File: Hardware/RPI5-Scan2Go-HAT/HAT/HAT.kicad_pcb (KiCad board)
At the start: 2 copper layers, 76 x 96.5 mm, 35 parts, among them J1 RPi_GPIO, J10 Conn_01x02_Socket, J12 Conn_01x02_Socket, J13 Conn_01x02_Socket, J14 Conn_01x02_Socket, J15 Jack-DC 5V, J18 Conn_01x02_Socket, J19 Conn_01x02_Socket, J2 Conn_01x04_Socket, J20 Conn_01x05_Socket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

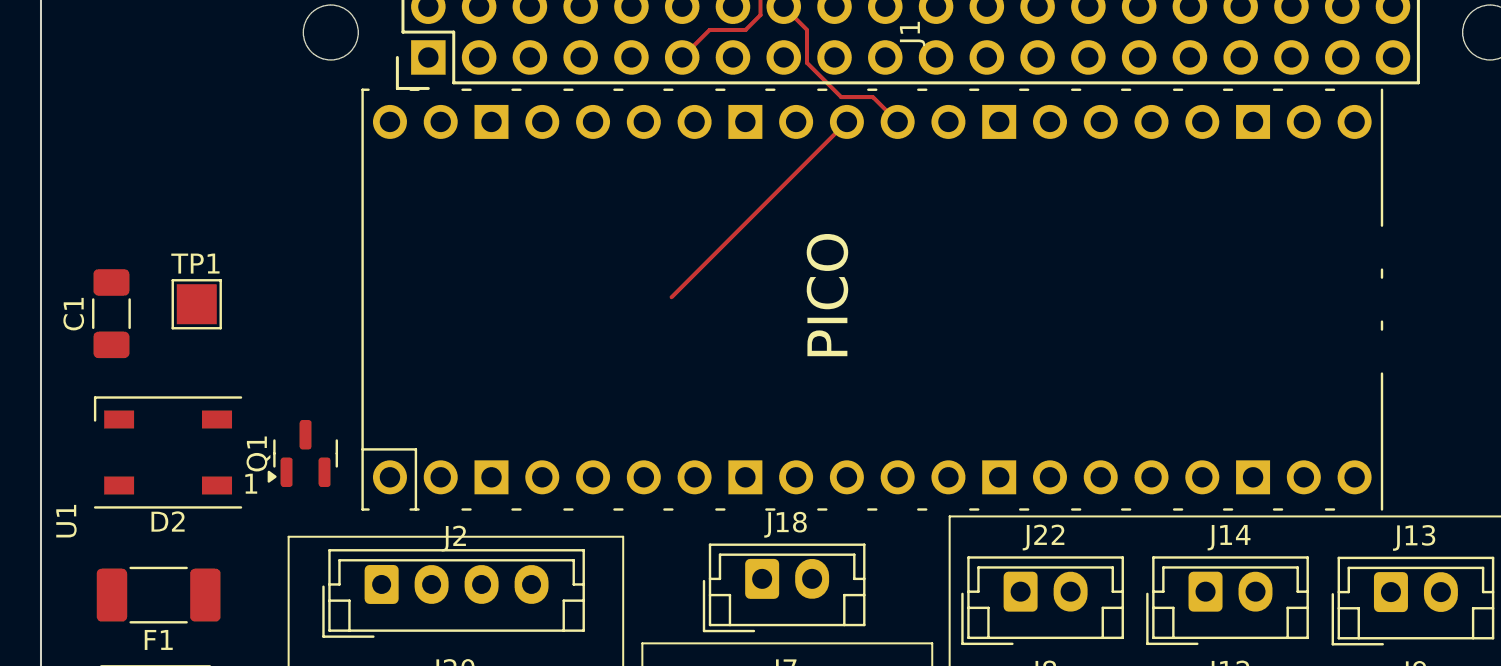
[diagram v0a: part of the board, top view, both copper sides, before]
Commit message: removed 5V from barel to pi and pico
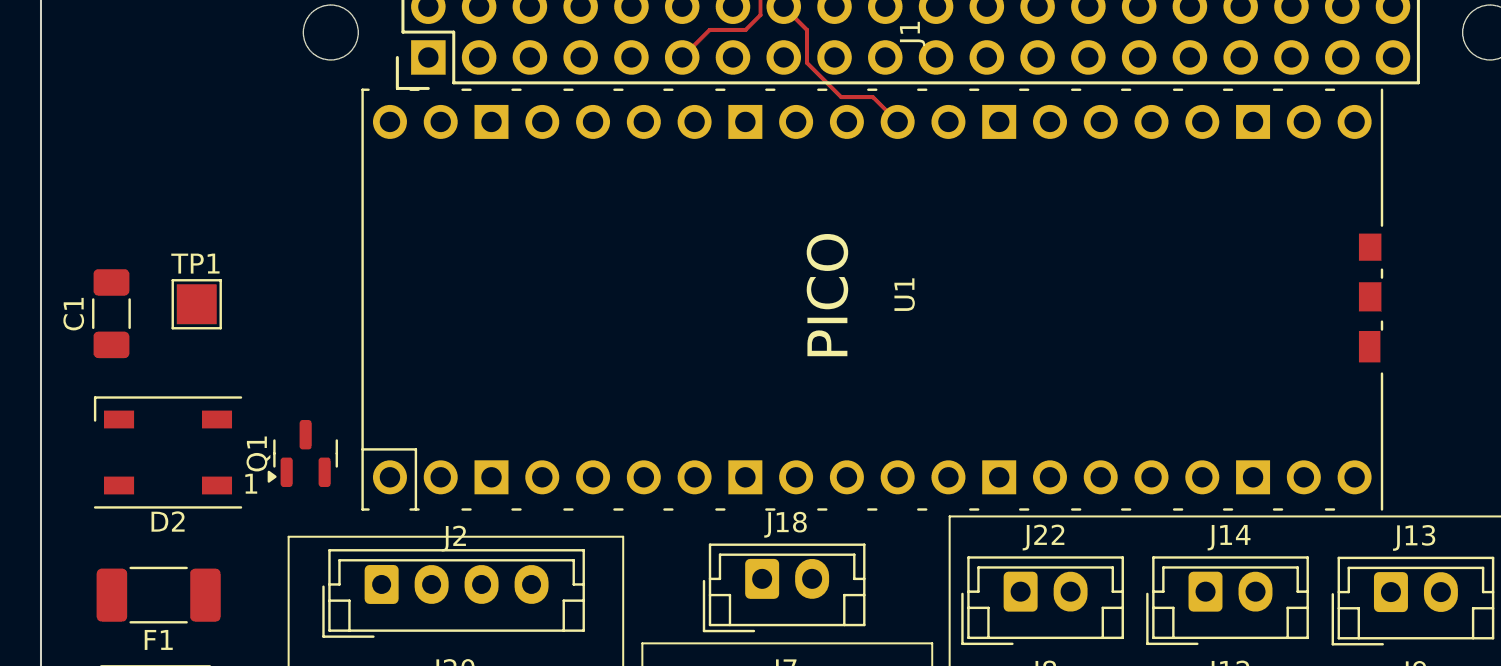
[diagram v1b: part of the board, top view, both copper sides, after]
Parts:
- F1: value 6A -> 10 A
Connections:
- D2 pad 1: +5V -> /VBUS
- J1 pad 2: +5V -> unconnected-(J1-5V-Pad2)
- J1 pad 4: +5V -> unconnected-(J1-5V-Pad4)
- J21 pad 4: Net-(J21-Pin_4) -> GND
- J23 pad 4: +5V -> /VBUS
- J7 pad 4: +5V -> /VBUS
- U1 pad 36: Net-(J21-Pin_4) -> unconnected-(U1-3V3-Pad36)
- U1 pad 39: Net-(Q1-S) -> unconnected-(U1-VSYS-Pad39)
- U1 pad 40: Net-(Q1-G) -> /VBUS
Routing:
- net Net-(J20-Pin_5): track 12.4 -> 0.00 mm
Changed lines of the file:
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@@
 	(net 16 "Net-(J18-Pin_1)")
 	(net 17 "Net-(J18-Pin_2)")
-	(net 18 "Net-(J21-Pin_4)")
+	(net 18 "/VBUS")
 	(net 19 "Net-(Q1-G)")
 	(net 20 "Net-(Q1-S)")
@@
 	(net 76 "unconnected-(J3-SHDN-Pad8)")
 	(net 77 "unconnected-(J3-SYNC0-Pad6)")
+	(net 78 "unconnected-(J1-5V-Pad2)")
+	(net 79 "unconnected-(J1-5V-Pad4)")
+	(net 80 "unconnected-(U1-3V3-Pad36)")
+	(net 81 "unconnected-(U1-VSYS-Pad39)")
+	(net 82 "unconnected-(U1-GND-Pad42)")
+	(net 83 "unconnected-(U1-SWDIO-Pad43)")
+	(net 84 "unconnected-(U1-SWCLK-Pad41)")
 	(footprint "SamacSys_Parts:DIOM5436X261N"
 		(layer "F.Cu")
@@
 			(layers "*.Cu" "*.Mask")
 			(remove_unused_layers no)
-			(net 4 "+5V")
+			(net 18 "/VBUS")
 			(pinfunction "Pin_4")
 			(pintype "passive")
@@
 			(layers "*.Cu" "*.Mask")
 			(remove_unused_layers no)
-			(net 4 "+5V")
+			(net 18 "/VBUS")
 			(pinfunction "Pin_4")
 			(pintype "passive")
@@
 			)
 		)
-		(property "Value" "6A"
+		(property "Value" "10 A"
 			(at 0 2.28 180)
 			(layer "F.Fab")
@@
 		(tags "Through hole pin header THT 2x20 2.54mm double row")
 		(property "Reference" "U1"
-			(at -11.08 -40.2877 -90)
+			(at 0.2532 1.647 -90)
 			(layer "F.SilkS")
 			(effects
@@
 		)
 		(property "Value" "Pico"
-			(at -11.13 -38.3787 -90)
+			(at 0.2032 3.556 -90)
 			(layer "F.Fab")
 			(effects
@@
 		)
 		(fp_line
+			(start 11 -26)
+			(end 11 26)
+			(stroke
+				(width 0.12)
+				(type solid)
+			)
+			(layer "F.CrtYd")
+		)
+		(fp_line
+			(start -11 -26)
+			(end 11 -26)
+			(stroke
+				(width 0.12)
+				(type solid)
+			)
+			(layer "F.CrtYd")
+		)
+		(fp_line
+			(start 11 26)
+			(end -11 26)
+			(stroke
+				(width 0.12)
+				(type solid)
+			)
+			(layer "F.CrtYd")
+		)
+		(fp_line
+			(start -11 26)
+			(end -11 -26)
+			(stroke
+				(width 0.12)
+				(type solid)
+			)
+			(layer "F.CrtYd")
+		)
+		(fp_line
 			(start 10.5 -25.5)
 			(end 10.5 25.5)
@@
 			(layers "*.Cu" "*.Mask")
 			(remove_unused_layers no)
-			(net 18 "Net-(J21-Pin_4)")
+			(net 80 "unconnected-(U1-3V3-Pad36)")
 			(pinfunction "3V3")
-			(pintype "unspecified")
+			(pintype "unspecified+no_connect")
 		)
 		(pad "37" thru_hole oval
@@
 			(layers "*.Cu" "*.Mask")
 			(remove_unused_layers no)
-			(net 20 "Net-(Q1-S)")
+			(net 81 "unconnected-(U1-VSYS-Pad39)")
 			(pinfunction "VSYS")
-			(pintype "unspecified")
+			(pintype "unspecified+no_connect")
 		)
 		(pad "40" thru_hole oval
@@
 			(layers "*.Cu" "*.Mask")
 			(remove_unused_layers no)
-			(net 19 "Net-(Q1-G)")
+			(net 18 "/VBUS")
 			(pinfunction "VBUS")
 			(pintype "unspecified")
 		)
+		(pad "41" smd rect
+			(at -2.286 25.1968 180)
+			(size 1.08 1.5612)
+			(drill
+				(offset 0.31 -0.0694)
+			)
+			(layers "F.Cu" "F.Paste")
+			(net 84 "unconnected-(U1-SWCLK-Pad41)")
+			(pinfunction "SWCLK")
+			(pintype "input+no_connect")
+		)
+		(pad "42" smd rect
+			(at 0.254 25.1968 180)
+			(size 1.1308 1.4596)
+			(drill
+				(offset 0.2846 -0.1202)
+			)
+			(layers "F.Cu" "F.Mask")
+			(net 82 "unconnected-(U1-GND-Pad42)")
+			(pinfunction "GND")
+			(pintype "power_in+no_connect")
+		)
+		(pad "43" smd rect
+			(at 2.794 25.1968 180)
+			(size 1.1308 1.358)
+			(drill
+				(offset 0.2846 -0.171)
+			)
+			(layers "F.Cu" "F.Mask")
+			(net 83 "unconnected-(U1-SWDIO-Pad43)")
+			(pinfunction "SWDIO")
+			(pintype "bidirectional+no_connect")
+		)
 		(model "${KICAD8_3DMODEL_DIR}/Connector_PinSocket_2.54mm.3dshapes/PinSocket_1x20_P2.54mm_Vertical.step"
 			(offset
@@
 			(layers "*.Cu" "*.Mask" "F.SilkS")
 			(remove_unused_layers no)
-			(net 4 "+5V")
+			(net 78 "unconnected-(J1-5V-Pad2)")
 			(pinfunction "5V")
-			(pintype "power_in")
+			(pintype "power_in+no_connect")
 		)
 		(pad "3" thru_hole oval
@@
 			(layers "*.Cu" "*.Mask" "F.SilkS")
 			(remove_unused_layers no)
-			(net 4 "+5V")
+			(net 79 "unconnected-(J1-5V-Pad4)")
 			(pinfunction "5V")
-			(pintype "power_in")
+			(pintype "power_in+no_connect")
 		)
 		(pad "5" thru_hole oval
@@
 			(layers "*.Cu" "*.Mask")
 			(remove_unused_layers no)
-			(net 18 "Net-(J21-Pin_4)")
+			(net 3 "GND")
 			(pinfunction "Pin_4")
 			(pintype "passive")
@@
 			(size 1.5 0.9)
 			(layers "F.Cu" "F.Paste" "F.Mask")
-			(net 4 "+5V")
+			(net 18 "/VBUS")
 			(pinfunction "VDD")
 			(pintype "power_in")
@@
 	)
 	(segment
-		(start 147.4118 100.3798)
-		(end 138.6418 109.1498)
-		(width 0.2)
-		(layer "F.Cu")
-		(net 28)
-	)
-	(segment

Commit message: V0.1 of pcb finished (To be reviewed)
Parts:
- removed ? (x4): , RPi_Hat:RPi_Hat_Mounting_Hole
- removed Q1: DMG2305UX, Package_TO_SOT_SMD:SOT-23
- added H1: MountingHole, , F.Cu at (179.6, 144.9)
- added H2: MountingHole, , F.Cu at (121.6, 144.9)
- added H3: MountingHole, , F.Cu at (121.6, 95.9)
- added H4: MountingHole, , F.Cu at (179.6, 95.9)
- moved TP1 3.81 mm to (116.6, 106.1)
- moved C1 2.27 mm to (112.3, 111.5), turned to 180 degrees
- moved D2 0.50 mm to (114.0, 116.8)
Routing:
- net +5V: track 0.00 -> 177.7 mm
- net /VBUS: track 0.00 -> 76.8 mm, vias 0 -> 1
- net Net-(J5-Pin_2): track 0.00 -> 74.9 mm, vias 0 -> 1
- net Net-(J2-Pin_4): track 0.00 -> 68.5 mm
- net Net-(J2-Pin_3): track 0.00 -> 66.0 mm, vias 0 -> 3
- net Net-(J2-Pin_2): track 0.00 -> 65.1 mm, vias 0 -> 2
- net Net-(D2-DIN): track 0.00 -> 63.3 mm, vias 0 -> 2
- net Net-(J2-Pin_1): track 0.00 -> 53.4 mm, vias 0 -> 2
- net Net-(J20-Pin_3): track 0.00 -> 44.6 mm
- net Net-(J20-Pin_1): track 0.00 -> 44.6 mm
- net Net-(J20-Pin_2): track 0.00 -> 42.3 mm
- net Net-(J20-Pin_4): track 0.00 -> 41.6 mm, vias 0 -> 1
- net Net-(J24-Pin_2): track 0.00 -> 41.3 mm
- net Net-(J19-Pin_1): track 0.00 -> 40.1 mm
- net Net-(J9-Pin_2): track 0.00 -> 40.1 mm
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- added copper zone on B.Cu, net GND
- added copper zone on F.Cu, net GND

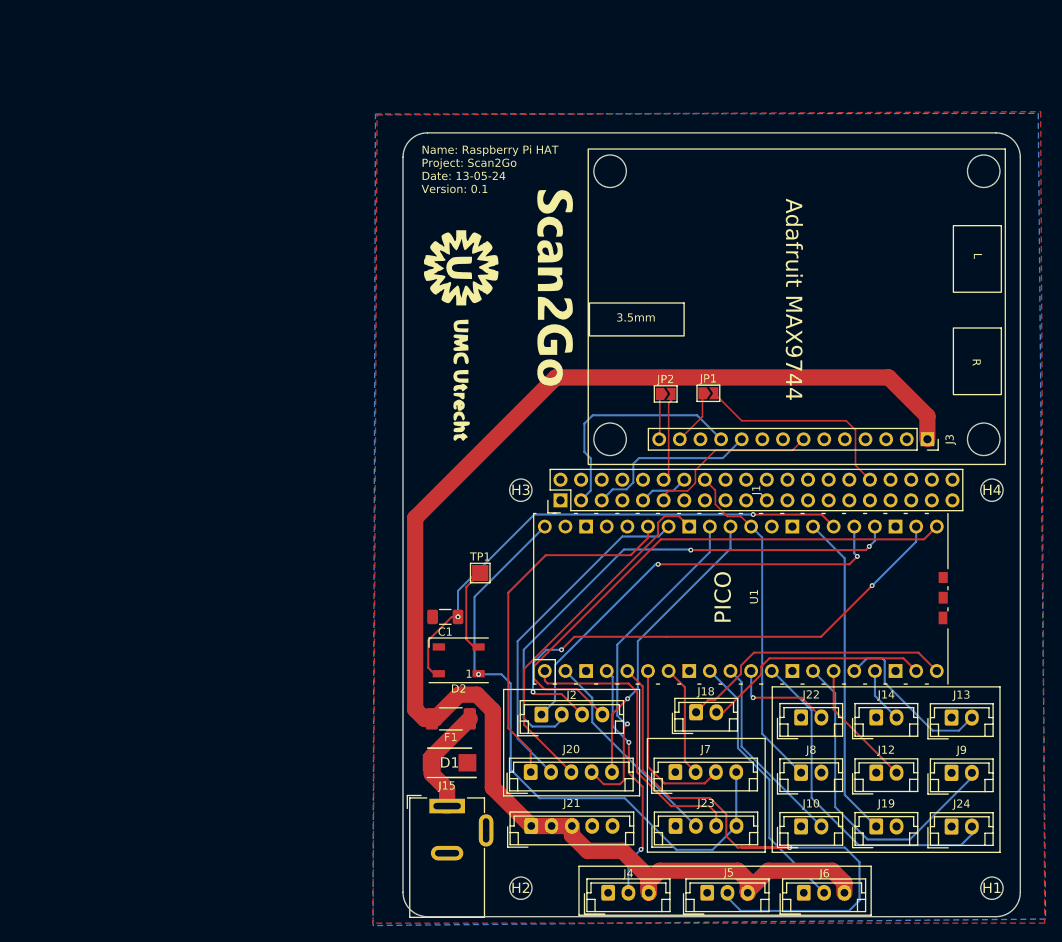
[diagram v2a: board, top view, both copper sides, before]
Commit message: Silkscreen improvements and additions
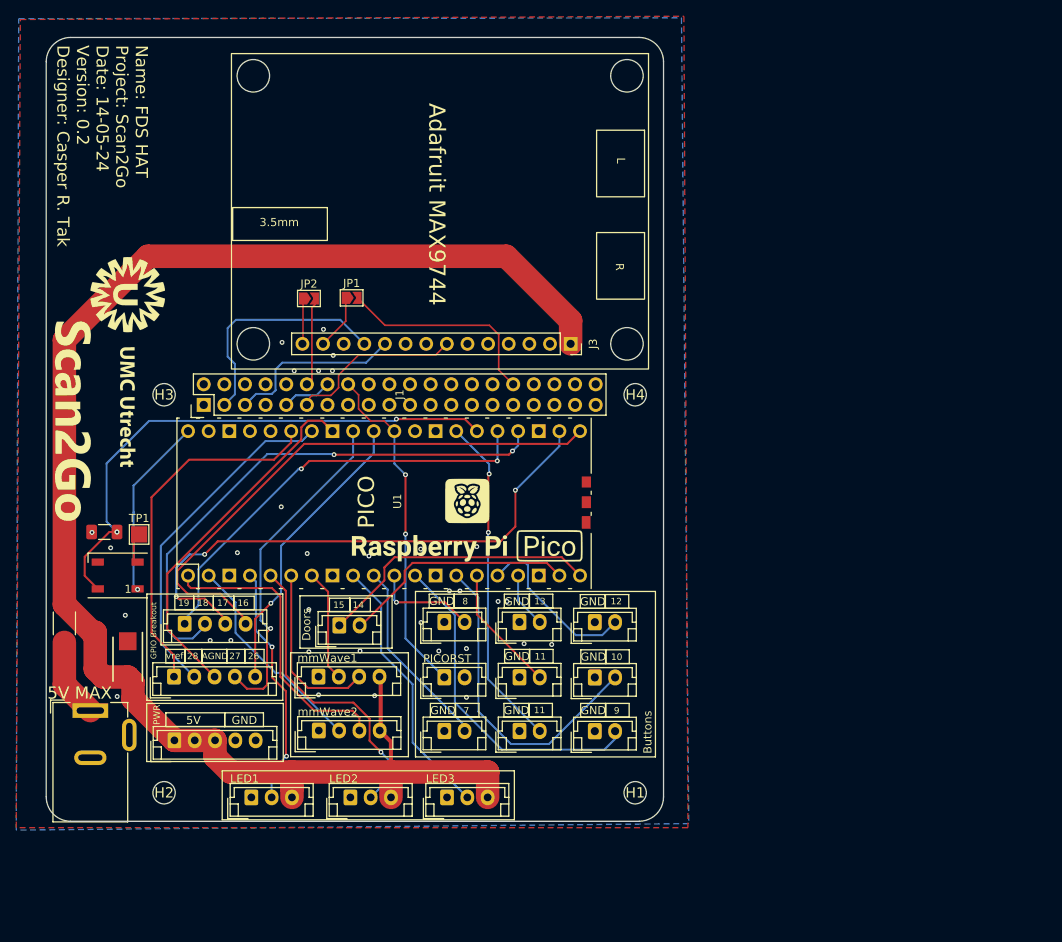
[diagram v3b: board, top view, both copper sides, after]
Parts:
- removed the G*** at (119.7, 73.9)
- added G***: LOGO, LOGO, F.Cu at (73.2, 80.1)
- added G***: LOGO, LOGO, F.Cu at (114.8, 99.2)
- added G***: LOGO, LOGO, F.Cu at (65.8, 87.2)
- added G***: LOGO, LOGO, B.Cu at (111.0, 55.0)
- added G***: LOGO, LOGO, B.Cu at (119.8, 61.0)
- added G***: LOGO, LOGO, B.Cu at (103.8, 96.7)
- moved F1 49.0 mm to (65.4, 112.3), turned to 90 degrees
- moved J1 45.5 mm to (106.7, 84.1)
- moved J10 45.5 mm to (112.2, 125.5)
- moved J13 45.5 mm to (130.7, 112.2)
- moved J14 45.5 mm to (121.4, 112.1)
- moved J19 45.5 mm to (121.4, 125.5)
- moved J22 45.5 mm to (112.2, 112.1)
- moved J24 45.5 mm to (130.7, 125.6)
- moved J4 45.5 mm to (88.4, 133.7)
- moved J9 45.5 mm to (130.7, 119.0)
- moved U1 45.5 mm to (104.8, 97.5)
- moved J12 45.5 mm to (121.4, 118.9)
- moved J15 45.5 mm to (68.6, 123.0)
- moved J8 45.5 mm to (112.2, 118.9)
- moved H2 45.5 mm to (77.7, 133.2)
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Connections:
- D1 pad 2: Net-(D1-K) -> +5V
- F1 pad 1: Net-(D1-K) -> Net-(F1-Pad1)
- J15 pad 1: Net-(D1-K) -> Net-(F1-Pad1)
- J19 pad 1: Net-(J19-Pin_1) -> GND
- J19 pad 2: GND -> Net-(J19-Pin_2)
- J23 pad 4: /VBUS -> +5V
- J7 pad 4: /VBUS -> +5V
- U1 pad 27: Net-(J19-Pin_1) -> Net-(J19-Pin_2)
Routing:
- net /VBUS: track 76.8 -> 22.6 mm
- net Net-(J19-Pin_2): track 0.00 -> 41.3 mm, vias 0 -> 2
- net Net-(J19-Pin_1): track 40.1 -> 0.00 mm
- net Net-(J5-Pin_2): track 74.9 -> 37.3 mm
- net +5V: track 177.7 -> 192.9 mm
- net Net-(D1-K): track 13.5 -> 0.00 mm
- net Net-(F1-Pad1): track 0.00 -> 9.72 mm
- net Net-(D2-DOUT): track 10.3 -> 3.75 mm
- net Net-(D2-DIN): track 63.3 -> 67.3 mm
- net Net-(J2-Pin_3): track 66.0 -> 68.6 mm
- net Net-(J2-Pin_2): track 65.1 -> 66.6 mm
- net Net-(J18-Pin_1): track 34.2 -> 35.0 mm
- net Net-(J18-Pin_2): track 28.6 -> 29.2 mm
- net Net-(J2-Pin_1): track 53.4 -> 52.8 mm
- net /PICORST: vias 0 -> 2
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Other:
- board text added: "10"
- board text added: "11"
- board text added: "12"
- board text added: "13"
- board text added: "14"
- board text added: "15"
- board text added: "16"
- board text added: "17"
- board text added: "18"
- board text added: "19"
- board text added: "26"
- board text added: "27"
- board text added: "28"
- board text added: "5V"
- board text added: "5V MAX"
- board text added: "7"
- board text added: "8"
- board text added: "9"
- board text added: "AGND"
- board text added: "Buttons"
- board text added: "Doors"
- board text added: "GND"
- board text added: "GPIO Breakout"
- board text added: "LED1"
- board text added: "LED2"
- board text added: "LED3"
- board text added: "Name: FDS HAT Project: Scan2Go Date: 14-05-24 Version: 0.2 Designer: Casper R. Tak"
- board text added: "PICORST"
- board text added: "PWR"
- board text added: "mmWave1"
- board text added: "mmWave2"
- board text added: "vref"
- board text removed: "Name: Raspberry Pi HAT Project: Scan2Go Date: 13-05-24 Version: 0.1"
